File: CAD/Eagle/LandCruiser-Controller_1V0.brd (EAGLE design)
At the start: 99 x 67.7 mm, 28 parts, among them U101 MEGA8-P, X301 I2C

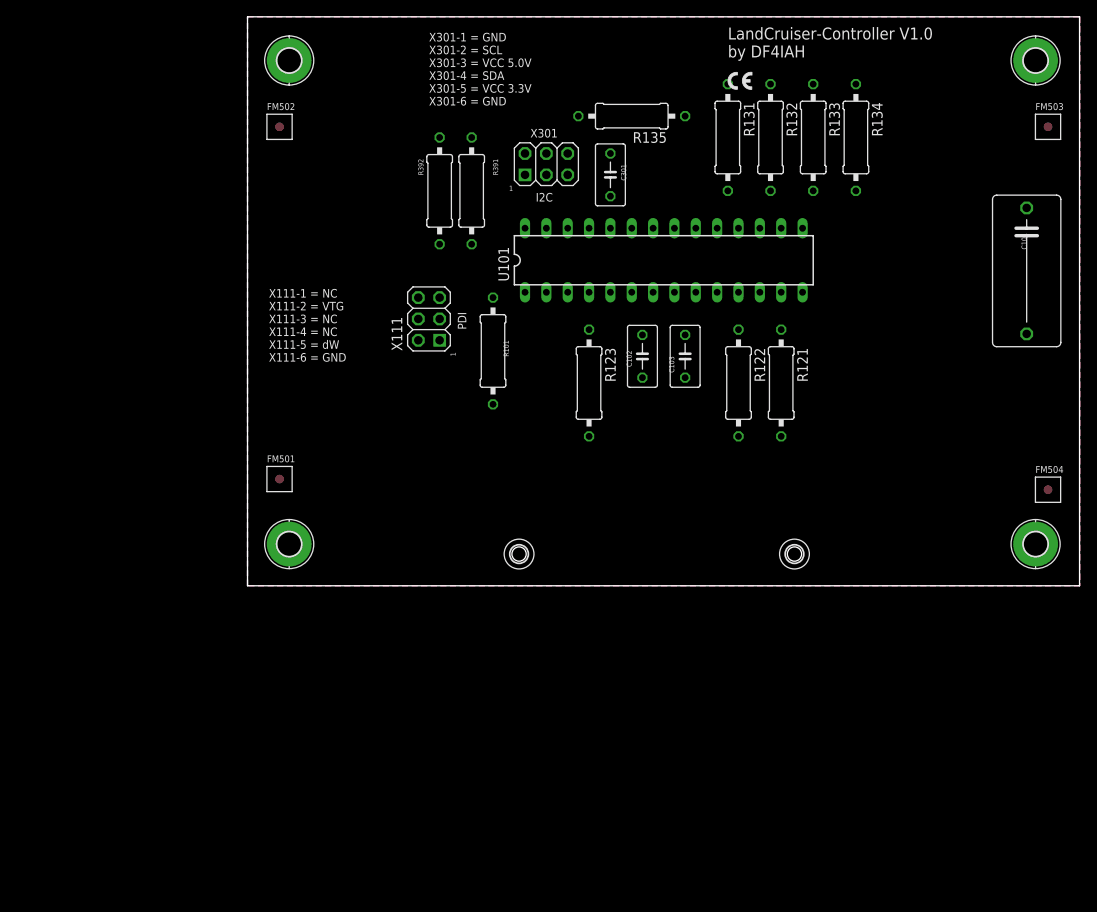
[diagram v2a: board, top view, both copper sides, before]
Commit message: HW - Linear voltage regulator 7805 added
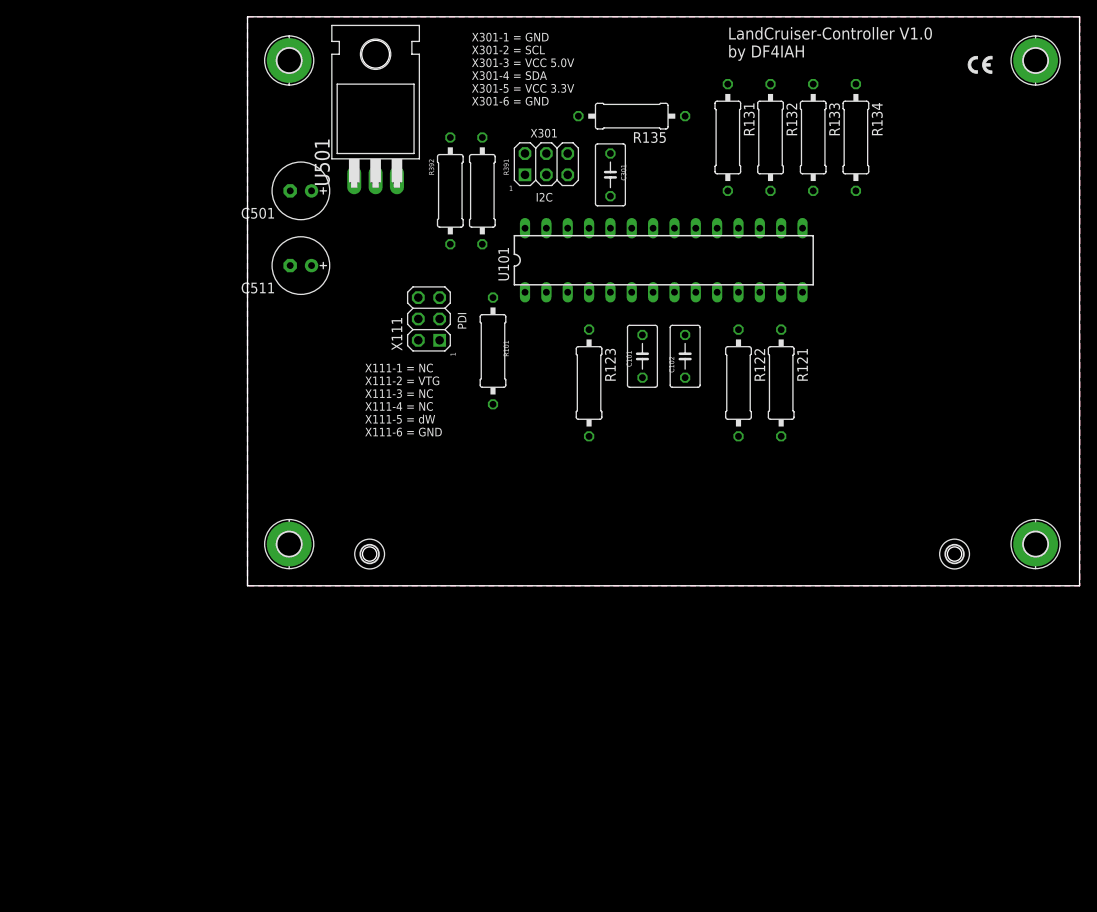
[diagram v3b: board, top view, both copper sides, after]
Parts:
- removed C103: 100pF, rcl:C050-035X075
- removed FM501, FM502, FM503, FM504: FIDUCIAL_MARK_1MM, df4iah_fiducial:FIDUCIAL_MARK_1MM
- removed H511, H512: MOUNT-HOLE1.7, df4iah_holes:1,7
- added C501, C511: 22uF, rcl:E2,5-7
- added H611, H612: MOUNT-HOLE1.7, df4iah_holes:1,7
- added U501: (no value), df4iah_powersupply:TO220H
- C101: value 22uF -> 100nF; device rcl:C150-084X183 -> rcl:C050-035X075
- C102: value 100nF -> 100pF
- moved C101 46.8 mm to (47.0, 27.3)
- moved C102 5.08 mm to (52.1, 27.3)
- moved R391 1.27 mm to (27.9, 47.0)
- moved R392 1.27 mm to (24.1, 47.0)
- renumbered H501 to H603, H502 to H601, H503 to H604, H504 to H602
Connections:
- new net +12V: C501.+, U501.1
- net +5V: now also C511.+, U501.3; no longer C102.1
- net AREF: now also C102.2; no longer C103.2
- net GND: now also C102.1, C501.-, C511.-; no longer C102.2, C103.1

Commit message: HW - Wire-to-Board connectors added
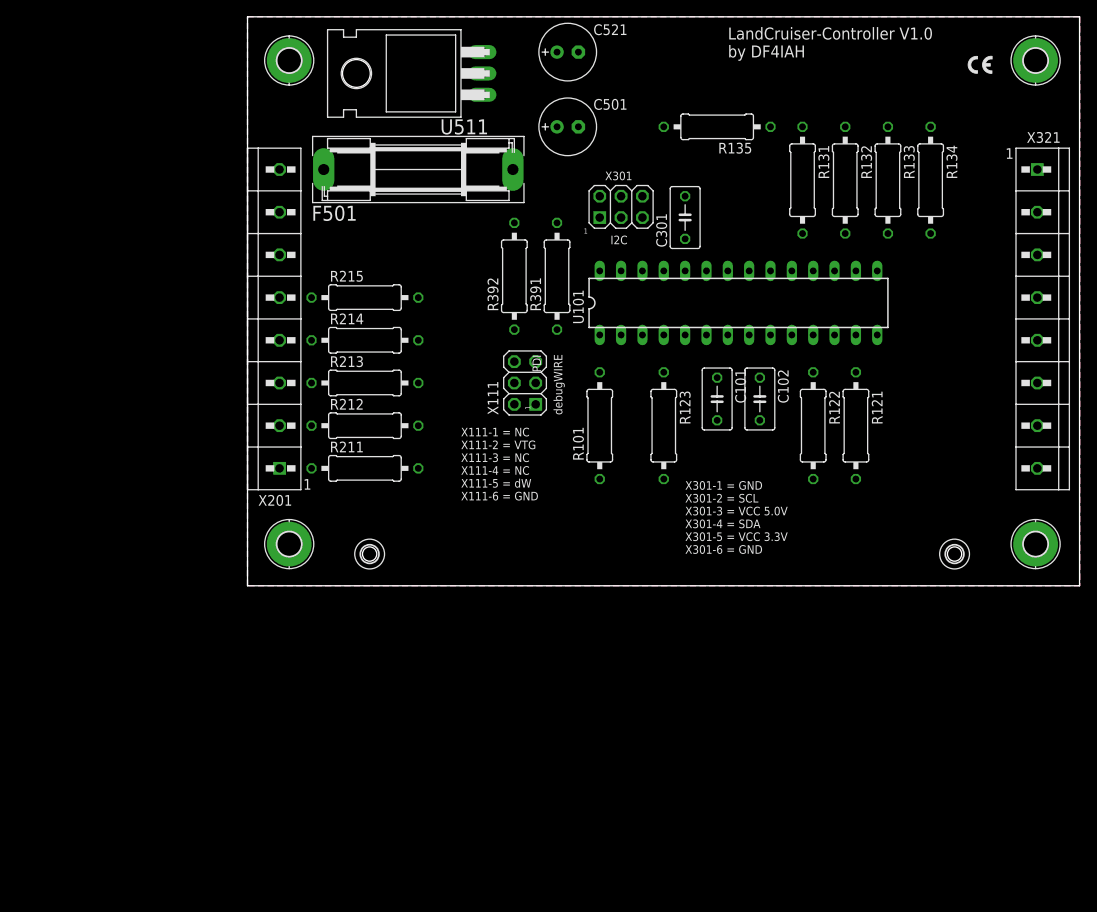
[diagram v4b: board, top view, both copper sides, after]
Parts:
- removed C511: 22uF, rcl:E2,5-7
- removed U501: (no value), df4iah_powersupply:TO220H
- added C521: 22uF, rcl:E2,5-7
- added F501: 500 mA (S), fuse:SH22,5
- added R211, R212, R213, R214, R215: 12kR, rcl:0309/12
- added U511: (no value), df4iah_powersupply:TO220H
- added X201, X321: WEIDMUELLER 1234600000, df4iah_connector:WIRE-TO-BOARD_5MM08_1X08
- moved C501 32.7 mm to (38.1, 54.6), turned to 0 degrees
- moved R101 15.5 mm to (41.9, 19.1)
- moved X111 13.7 mm to (33.0, 24.1)
- moved R391 13.5 mm to (36.8, 36.8)
- moved R392 12.7 mm to (31.8, 36.8)
- moved R131 10.2 mm to (66.0, 48.3)
- moved R132 10.2 mm to (71.1, 48.3)
- moved R135 10.2 mm to (55.9, 54.6)
- moved C301 10.2 mm to (52.1, 43.8)
- moved R133 10.2 mm to (76.2, 48.3)
- moved R134 10.2 mm to (81.3, 48.3)
- moved C101 10.2 mm to (55.9, 22.2)
- moved C102 10.2 mm to (61.0, 22.2)
- moved R121 10.2 mm to (72.4, 19.1)
- moved R122 10.2 mm to (67.3, 19.1)
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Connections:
- new net +UB: F501.1, X201.8
- new net N$1: R211.1, X201.1
- new net N$10: X321.5
- new net N$2: R212.1, X201.2
- new net N$3: R213.1, X201.3
- new net N$4: R214.1, X201.4
- new net N$5: R215.1, X201.5
- new net N$6: X321.1
- new net N$7: X321.2
- new net N$8: X321.3
- new net N$9: X321.4
- net +12V: now also F501.2, U511.1; no longer U501.1
- net +5V: now also C521.+, U511.3; no longer C511.+, U501.3
- net GND: now also C521.-, X201.7, X321.8; no longer C511.-
- net MP_KL: now also R211.2
- net MP_SA_G: now also R214.2
- net MP_SA_O: now also R215.2
- net MP_SK_G: now also R212.2
- net MP_SK_O: now also R213.2
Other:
- board text added: "debugWIRE"

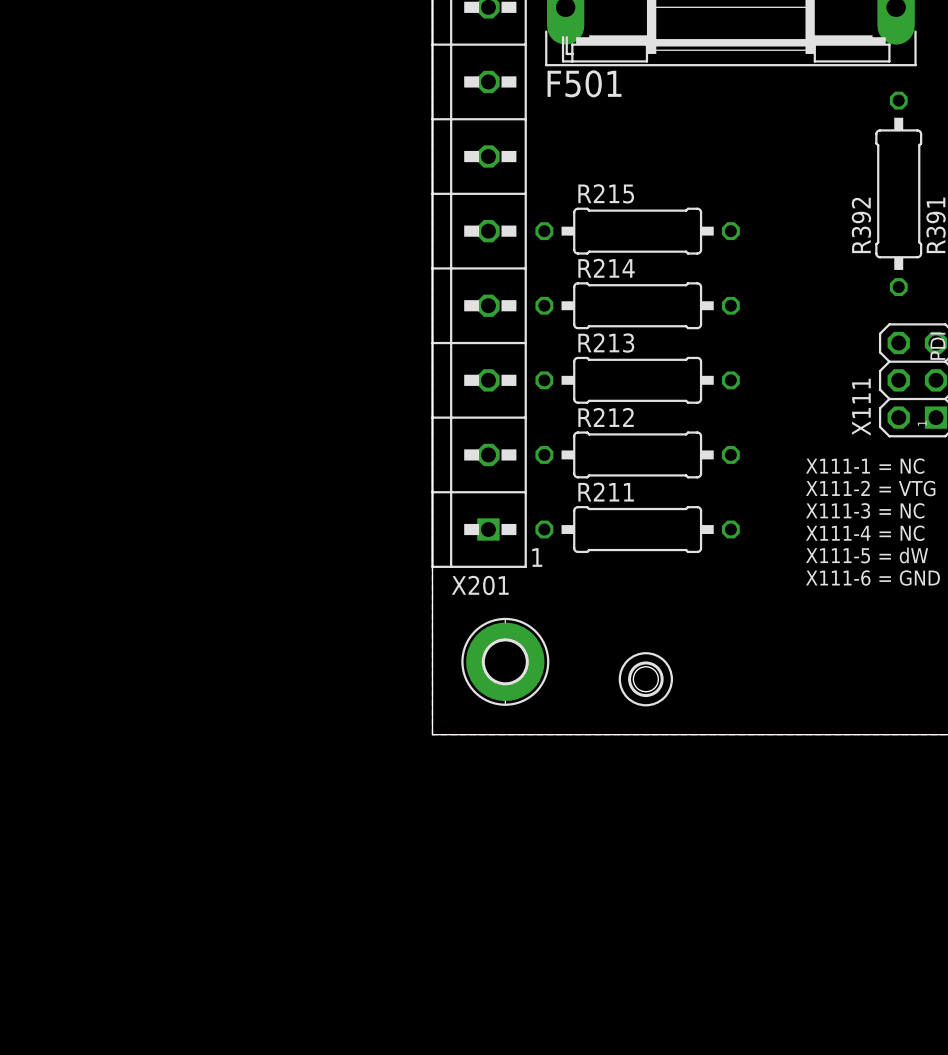
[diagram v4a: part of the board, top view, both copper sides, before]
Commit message: HW_V1.0 - ESD - circuits added
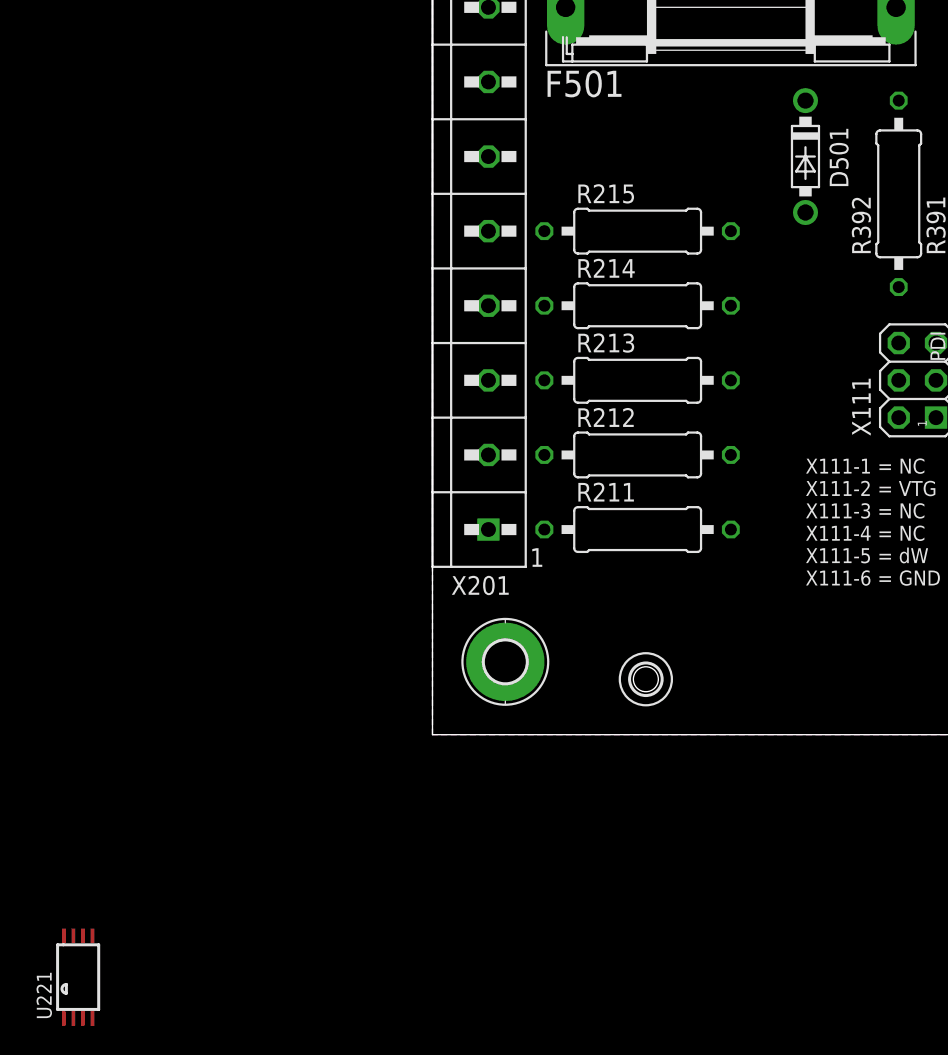
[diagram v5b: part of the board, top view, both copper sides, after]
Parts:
- added D501: 1N5817-B, df4iah_diode:DO41-7.6
- added U221: SN75240, df4iah_esd:TSSOP-8
- R211, R212, R213, R214, R215: value 12kR -> 56R
- U511: value (none) -> LM7805
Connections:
- net N$1 renamed ECU_FB
- net N$10 renamed M2
- net N$2 renamed SK_G
- net N$3 renamed SK_O
- net N$4 renamed SA_G
- net N$5 renamed SA_O
- net N$6 renamed KL
- net N$7 renamed PV_G
- net N$8 renamed PV_O
- net N$9 renamed M1
- net +12V: now also D501.C
- net GND: now also D501.A, U221.1, U221.3, U221.5, U221.7, U511.2
- net MP_FB: now also R211.2
- net MP_KL: no longer R211.2
- net MP_SA_G: now also U221.2
- net MP_SA_O: now also U221.4
- net MP_SK_G: now also U221.8
- net MP_SK_O: now also U221.6
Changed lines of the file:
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@@
 <element name="R123" library="rcl" package="0309/12" value="4k7R" x="49.53" y="19.05" rot="R270"/>
 <element name="X111" library="df4iah_connector" package="2X03" value="" x="33.02" y="24.13" rot="R90"/>
-<element name="U511" library="df4iah_powersupply" package="TO220H" value="" x="17.78" y="60.96" rot="R90"/>
+<element name="U511" library="df4iah_powersupply" package="TO220H" value="LM7805" x="17.78" y="60.96" rot="R90"/>
 <element name="C521" library="rcl" package="E2,5-7" value="22uF" x="38.1" y="63.5"/>
 <element name="C501" library="rcl" package="E2,5-7" value="22uF" x="38.1" y="54.61"/>
@@
 <attribute name="VALUE" x="6.35" y="53.975" size="1.27" layer="27" rot="R180"/>
 </element>
-<element name="R215" library="rcl" package="0309/12" value="12kR" x="13.97" y="34.29"/>
-<element name="R214" library="rcl" package="0309/12" value="12kR" x="13.97" y="29.21"/>
-<element name="R213" library="rcl" package="0309/12" value="12kR" x="13.97" y="24.13"/>
-<element name="R212" library="rcl" package="0309/12" value="12kR" x="13.97" y="19.05"/>
-<element name="R211" library="rcl" package="0309/12" value="12kR" x="13.97" y="13.97"/>
+<element name="R215" library="rcl" package="0309/12" value="56R" x="13.97" y="34.29"/>
+<element name="R214" library="rcl" package="0309/12" value="56R" x="13.97" y="29.21"/>
+<element name="R213" library="rcl" package="0309/12" value="56R" x="13.97" y="24.13"/>
+<element name="R212" library="rcl" package="0309/12" value="56R" x="13.97" y="19.05"/>
+<element name="R211" library="rcl" package="0309/12" value="56R" x="13.97" y="13.97"/>
 <element name="F501" library="fuse" package="SH22,5" value="500 mA (S)" x="20.32" y="49.53">
 <attribute name="MF" value="SCHURTER" x="20.32" y="49.53" size="1.778" layer="27" display="off"/>
@@
 </element>
 <element name="X321" library="df4iah_connector" package="WIRE-TO-BOARD_5MM08_1X08" value="WEIDMUELLER 1234600000" x="93.98" y="31.75"/>
+<element name="D501" library="df4iah_diode" package="DO41-7.6" value="1N5817-B" x="25.4" y="39.37" rot="R270"/>
+<element name="U221" library="df4iah_esd" package="TSSOP-8" value="SN75240" x="-24.13" y="-16.51"/>
 </elements>
 <signals>
@@
 <contactref element="X201" pad="7"/>
 <contactref element="X321" pad="8"/>
+<contactref element="D501" pad="A"/>
+<contactref element="U221" pad="3"/>
+<contactref element="U221" pad="1"/>
+<contactref element="U221" pad="5"/>
+<contactref element="U221" pad="7"/>
+<contactref element="U511" pad="2"/>
 <wire x1="81.28" y1="54.61" x2="93.77" y2="62.5" width="0" layer="19" extent="1-1"/>
 <wire x1="76.2" y1="54.61" x2="81.28" y2="54.61" width="0" layer="19" extent="1-1"/>
@@
 <wire x1="39.37" y1="54.61" x2="41.91" y2="43.815" width="0" layer="19" extent="1-1"/>
 <wire x1="39.37" y1="63.5" x2="39.37" y2="54.61" width="0" layer="19" extent="1-1"/>
-<wire x1="31.75" y1="26.67" x2="41.91" y2="43.815" width="0" layer="19" extent="1-1"/>
-<wire x1="3.81" y1="44.45" x2="31.75" y2="26.67" width="0" layer="19" extent="1-1"/>
-<wire x1="4.96" y1="62.5" x2="3.81" y2="44.45" width="0" layer="19" extent="1-1"/>
+<wire x1="27.94" y1="60.96" x2="39.37" y2="63.5" width="0" layer="19" extent="1-1"/>
+<wire x1="25.4" y1="35.56" x2="41.91" y2="43.815" width="0" layer="19" extent="1-1"/>
+<wire x1="31.75" y1="26.67" x2="25.4" y2="35.56" width="0" layer="19" extent="1-1"/>
+<wire x1="4.96" y1="62.5" x2="27.94" y2="60.96" width="0" layer="19" extent="1-1"/>
+<wire x1="3.81" y1="44.45" x2="4.96" y2="62.5" width="0" layer="19" extent="1-1"/>
 <wire x1="4.96" y1="4.96" x2="31.75" y2="26.67" width="0" layer="19" extent="1-1"/>
-<wire x1="93.77" y1="4.96" x2="60.96" y2="24.765" width="0" layer="19" extent="1-1"/>
-<wire x1="93.98" y1="13.97" x2="4.96" y2="4.96" width="0" layer="19" extent="1-1"/>
+<wire x1="-23.155" y1="-13.6969" x2="4.96" y2="4.96" width="0" layer="19" extent="1-1"/>
+<wire x1="-24.455" y1="-13.6969" x2="-23.155" y2="-13.6969" width="0" layer="19" extent="1-1"/>
+<wire x1="-23.805" y1="-19.3231" x2="-23.155" y2="-13.6969" width="0" layer="19" extent="1-1"/>
+<wire x1="-25.105" y1="-19.3231" x2="-23.805" y2="-19.3231" width="0" layer="19" extent="1-1"/>
+<wire x1="93.98" y1="13.97" x2="60.96" y2="24.765" width="0" layer="19" extent="1-1"/>
+<wire x1="93.77" y1="4.96" x2="93.98" y2="13.97" width="0" layer="19" extent="1-1"/>
 </signal>
 <signal name="+5V">
@@
 <contactref element="U101" pad="9"/>
 <contactref element="R212" pad="2"/>
+<contactref element="U221" pad="8"/>
 <wire x1="20.32" y1="19.05" x2="62.23" y2="29.845" width="0" layer="19" extent="1-1"/>
+<wire x1="-25.105" y1="-13.6969" x2="20.32" y2="19.05" width="0" layer="19" extent="1-1"/>
 </signal>
 <signal name="MP_FB">
 <contactref element="U101" pad="6"/>
 <contactref element="R123" pad="1"/>
+<contactref element="R211" pad="2"/>
 <wire x1="49.53" y1="25.4" x2="54.61" y2="29.845" width="0" layer="19" extent="1-1"/>
+<wire x1="20.32" y1="13.97" x2="49.53" y2="25.4" width="0" layer="19" extent="1-1"/>
 </signal>
 <signal name="MP_SK_O">
 <contactref element="U101" pad="10"/>
 <contactref element="R213" pad="2"/>
+<contactref element="U221" pad="6"/>
 <wire x1="20.32" y1="24.13" x2="64.77" y2="29.845" width="0" layer="19" extent="1-1"/>
+<wire x1="-23.805" y1="-13.6969" x2="20.32" y2="24.13" width="0" layer="19" extent="1-1"/>
 </signal>
 <signal name="MP_SA_G">
@@
 <contactref element="R122" pad="1"/>
 <contactref element="R214" pad="2"/>
+<contactref element="U221" pad="2"/>
 <wire x1="67.31" y1="25.4" x2="69.85" y2="29.845" width="0" layer="19" extent="1-1"/>
 <wire x1="20.32" y1="29.21" x2="67.31" y2="25.4" width="0" layer="19" extent="1-1"/>
+<wire x1="-24.455" y1="-19.3231" x2="20.32" y2="29.21" width="0" layer="19" extent="1-1"/>
 </signal>
 <signal name="MP_SA_O">
@@
 <contactref element="R121" pad="1"/>
 <contactref element="R215" pad="2"/>
+<contactref element="U221" pad="4"/>
 <wire x1="72.39" y1="25.4" x2="72.39" y2="29.845" width="0" layer="19" extent="1-1"/>
 <wire x1="20.32" y1="34.29" x2="72.39" y2="29.845" width="0" layer="19" extent="1-1"/>
+<wire x1="-23.155" y1="-19.3231" x2="20.32" y2="34.29" width="0" layer="19" extent="1-1"/>
 </signal>
 <signal name="MP_M2">
@@
 <contactref element="U101" pad="26"/>
 <contactref element="R135" pad="2"/>
-<contactref element="R211" pad="2"/>
 <wire x1="46.99" y1="37.465" x2="49.53" y2="54.61" width="0" layer="19" extent="1-1"/>
-<wire x1="20.32" y1="13.97" x2="46.99" y2="37.465" width="0" layer="19" extent="1-1"/>
 </signal>
 <signal name="+12V">
@@
 <contactref element="C501" pad="+"/>
 <contactref element="F501" pad="2"/>
+<contactref element="D501" pad="C"/>
 <wire x1="31.5722" y1="49.53" x2="36.83" y2="54.61" width="0" layer="19" extent="1-1"/>
 <wire x1="27.94" y1="58.42" x2="31.5722" y2="49.53" width="0" layer="19" extent="1-1"/>
-</signal>
-<signal name="N$1">
+<wire x1="25.4" y1="43.18" x2="31.5722" y2="49.53" width="0" layer="19" extent="1-1"/>
+</signal>
+<signal name="ECU_FB">
 <contactref element="X201" pad="1"/>
 <contactref element="R211" pad="1"/>
 <wire x1="3.81" y1="13.97" x2="7.62" y2="13.97" width="0" layer="19" extent="1-1"/>
 </signal>
-<signal name="N$2">
+<signal name="SK_G">
 <contactref element="X201" pad="2"/>
 <contactref element="R212" pad="1"/>
 <wire x1="3.81" y1="19.05" x2="7.62" y2="19.05" width="0" layer="19" extent="1-1"/>
 </signal>
-<signal name="N$3">
+<signal name="SK_O">
 <contactref element="X201" pad="3"/>
 <contactref element="R213" pad="1"/>
 <wire x1="3.81" y1="24.13" x2="7.62" y2="24.13" width="0" layer="19" extent="1-1"/>
 </signal>
-<signal name="N$4">
+<signal name="SA_G">
 <contactref element="X201" pad="4"/>
 <contactref element="R214" pad="1"/>
 <wire x1="3.81" y1="29.21" x2="7.62" y2="29.21" width="0" layer="19" extent="1-1"/>
 </signal>
-<signal name="N$5">
+<signal name="SA_O">
 <contactref element="X201" pad="5"/>
 <contactref element="R215" pad="1"/>
@@
 <wire x1="3.81" y1="49.53" x2="9.0678" y2="49.53" width="0" layer="19" extent="1-1"/>
 </signal>
-<signal name="N$6">
+<signal name="KL">
 <contactref element="X321" pad="1"/>
 </signal>
-<signal name="N$7">
+<signal name="PV_G">
 <contactref element="X321" pad="2"/>
 </signal>
-<signal name="N$8">
+<signal name="PV_O">
 <contactref element="X321" pad="3"/>
 </signal>
-<signal name="N$9">
+<signal name="M1">
 <contactref element="X321" pad="4"/>
 </signal>
-<signal name="N$10">
+<signal name="M2">
 <contactref element="X321" pad="5"/>
 </signal>
